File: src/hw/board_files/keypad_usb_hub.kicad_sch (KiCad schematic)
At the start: 2 parts, among them U1 MDBT50Q-1MV2, U2 IS31FL3731-SA

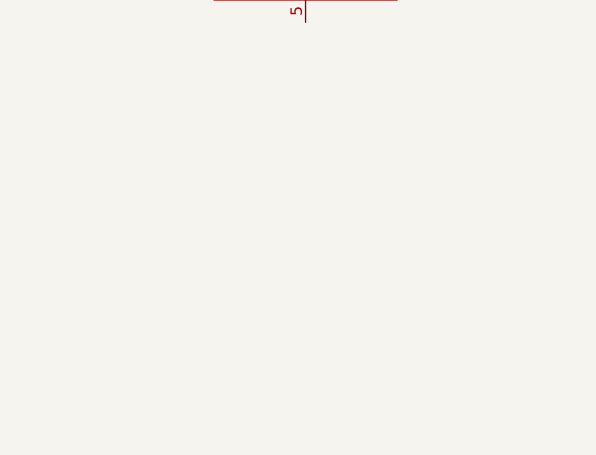
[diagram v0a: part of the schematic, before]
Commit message: Changed some ICs
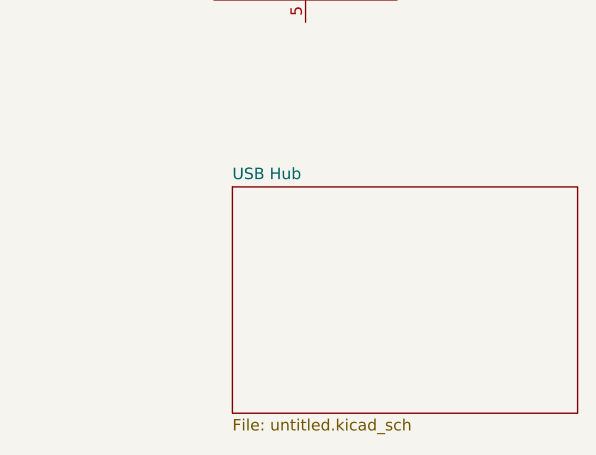
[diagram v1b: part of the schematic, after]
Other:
- added sheet USB Hub (untitled.kicad_sch)
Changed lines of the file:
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@@
+		)
+	)
+	(sheet
+		(at 188.722 109.728)
+		(size 38.354 25.146)
+		(exclude_from_sim no)
+		(in_bom yes)
+		(on_board yes)
+		(dnp no)
+		(fields_autoplaced yes)
+		(stroke
+			(width 0.1524)
+			(type solid)
+		)
+		(fill
+			(color 0 0 0 0.0000)
+		)
+		(property "Sheetname" "USB Hub"
+			(at 188.722 109.0164 0)
+			(effects
+				(font
+					(size 1.27 1.27)
+				)
+				(justify left bottom)
+			)
+		)
+		(property "Sheetfile" "untitled.kicad_sch"
+			(at 188.722 135.4586 0)
+			(effects
+				(font
+					(size 1.27 1.27)
+				)
+				(justify left top)
+			)
+		)
+		(instances
+			(project "keypad_usb_hub"
+				(path "/62136966-d911-451f-9518-a7827b282fe3"
+					(page "2")
+				)
+			)
 		)
 	)

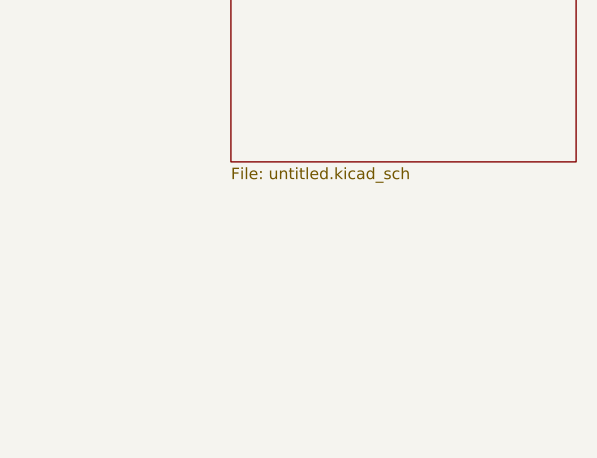
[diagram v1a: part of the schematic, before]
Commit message: Made USB hub symbol
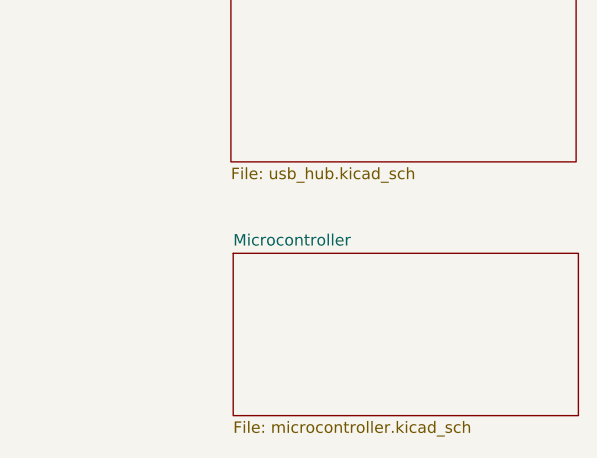
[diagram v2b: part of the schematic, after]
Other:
- added sheet Microcontroller (microcontroller.kicad_sch)
- sheet USB Hub: file untitled.kicad_sch -> usb_hub.kicad_sch
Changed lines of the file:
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@@
 			)
 		)
-		(property "Sheetfile" "untitled.kicad_sch"
+		(property "Sheetfile" "usb_hub.kicad_sch"
 			(at 188.722 135.4586 0)
 			(effects
@@
 				)
 			)
+		)
+	)
+	(sheet
+		(at 188.976 145.034)
+		(size 38.354 18.034)
+		(exclude_from_sim no)
+		(in_bom yes)
+		(on_board yes)
+		(dnp no)
+		(fields_autoplaced yes)
+		(stroke
+			(width 0.1524)
+			(type solid)
+		)
+		(fill
+			(color 0 0 0 0.0000)
+		)
+		(property "Sheetname" "Microcontroller"
+			(at 188.976 144.3224 0)
+			(effects
+				(font
+					(size 1.27 1.27)
+				)
+				(justify left bottom)
+			)
+		)
+		(property "Sheetfile" "microcontroller.kicad_sch"
+			(at 188.976 163.6526 0)
+			(effects
+				(font
+					(size 1.27 1.27)
+				)
+				(justify left top)
+			)
+		)
+		(instances
+			(project "keypad_usb_hub"
+				(path "/62136966-d911-451f-9518-a7827b282fe3"
+					(page "3")
+				)
+			)

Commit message: Schematic progress
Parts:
- removed U1: MDBT50Q-1MV2, RF_Module:Raytac_MDBT50Q, symbol RF_Module:MDBT50Q-1MV2
- removed U2: IS31FL3731-SA, Package_SO:SSOP-28_5.3x10.2mm_P0.65mm, symbol Driver_LED:IS31FL3731-SA
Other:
- sheet USB Hub renamed USB Hub Controller
- added sheet Power (power.kicad_sch)
- added sheet Receptacles (receptacles.kicad_sch)

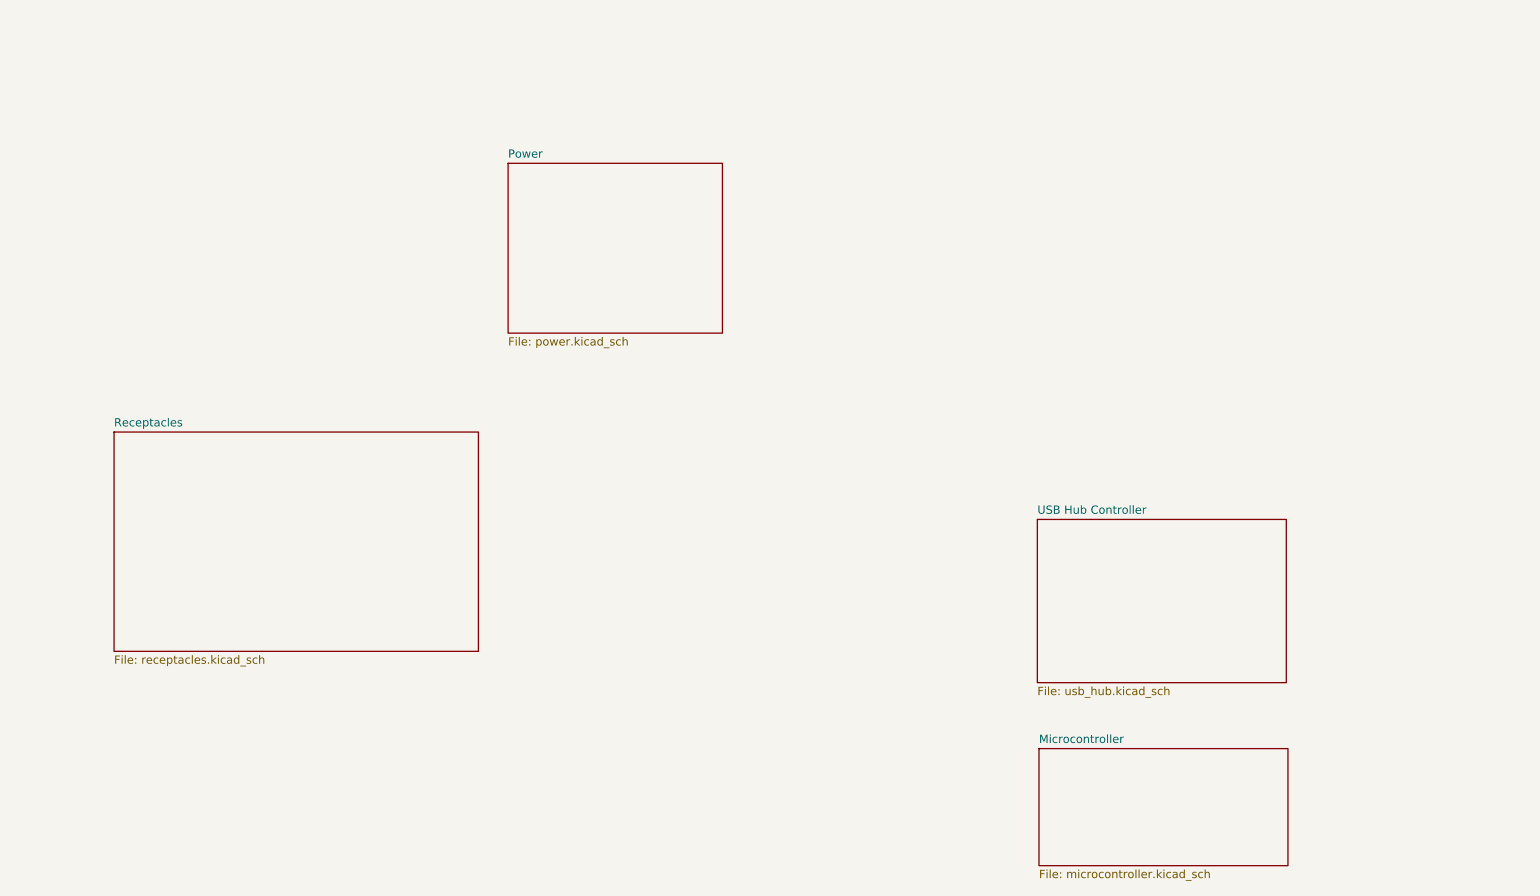
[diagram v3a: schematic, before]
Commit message: Finishing schematic. Need to review and clean up
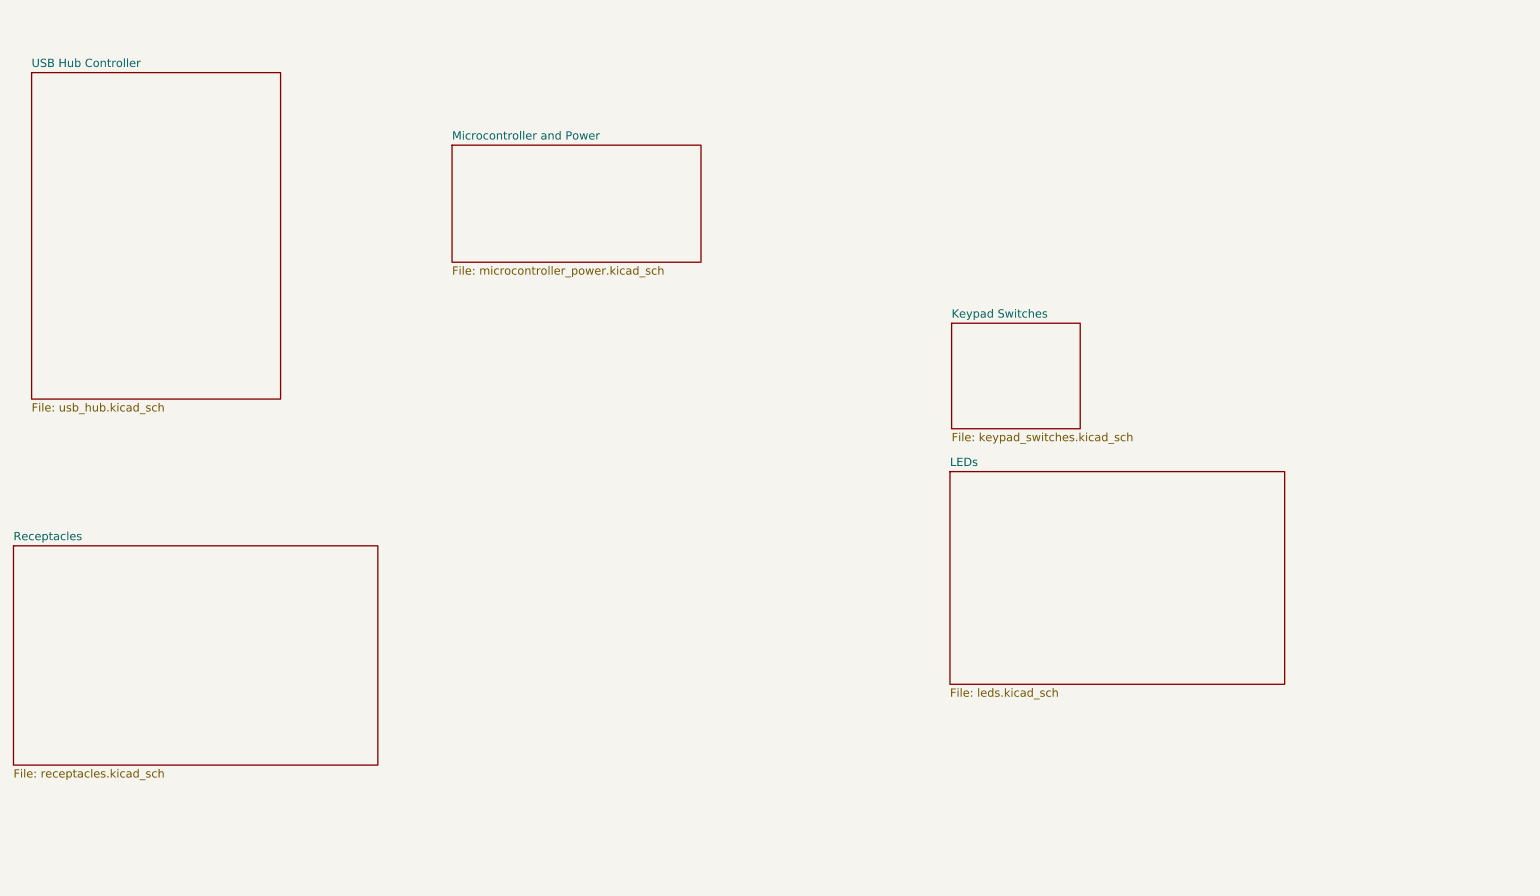
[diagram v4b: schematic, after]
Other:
- sheet Microcontroller renamed Microcontroller and Power
- removed sheet Power
- added sheet Keypad Switches (keypad_switches.kicad_sch)
- added sheet LEDs (leds.kicad_sch)
- sheet Microcontroller and Power: file microcontroller.kicad_sch -> microcontroller_power.kicad_sch
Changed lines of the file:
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@@
 	)
 	(sheet
-		(at 188.722 109.728)
-		(size 38.354 25.146)
+		(at 175.26 102.362)
+		(size 51.562 32.766)
+		(exclude_from_sim no)
+		(in_bom yes)
+		(on_board yes)
+		(dnp no)
+		(fields_autoplaced yes)
+		(stroke
+			(width 0.1524)
+			(type solid)
+		)
+		(fill
+			(color 0 0 0 0.0000)
+		)
+		(property "Sheetname" "LEDs"
+			(at 175.26 101.6504 0)
+			(effects
+				(font
+					(size 1.27 1.27)
+				)
+				(justify left bottom)
+			)
+		)
+		(property "Sheetfile" "leds.kicad_sch"
+			(at 175.26 135.7126 0)
+			(effects
+				(font
+					(size 1.27 1.27)
+				)
+				(justify left top)
+			)
+		)
+		(instances
+			(project "keypad_usb_hub"
+				(path "/62136966-d911-451f-9518-a7827b282fe3"
+					(page "5")
+				)
+			)
+		)
+	)
+	(sheet
+		(at 33.782 40.894)
+		(size 38.354 50.292)
 		(exclude_from_sim no)
 		(in_bom yes)
@@
 		)
 		(property "Sheetname" "USB Hub Controller"
-			(at 188.722 109.0164 0)
+			(at 33.782 40.1824 0)
 			(effects
 				(font
@@
 		)
 		(property "Sheetfile" "usb_hub.kicad_sch"
-			(at 188.722 135.4586 0)
+			(at 33.782 91.7706 0)
 			(effects
 				(font
@@
 	)
 	(sheet
-		(at 188.976 145.034)
+		(at 98.552 52.07)
 		(size 38.354 18.034)
 		(exclude_from_sim no)
@@
 			(color 0 0 0 0.0000)
 		)
-		(property "Sheetname" "Microcontroller"
-			(at 188.976 144.3224 0)
-			(effects
-				(font
-					(size 1.27 1.27)
-				)
-				(justify left bottom)
-			)
-		)
-		(property "Sheetfile" "microcontroller.kicad_sch"
-			(at 188.976 163.6526 0)
+		(property "Sheetname" "Microcontroller and Power"
+			(at 98.552 51.3584 0)
+			(effects
+				(font
+					(size 1.27 1.27)
+				)
+				(justify left bottom)
+			)
+		)
+		(property "Sheetfile" "microcontroller_power.kicad_sch"
+			(at 98.552 70.6886 0)
 			(effects
 				(font
@@
 	)
 	(sheet
-		(at 46.482 96.266)
+		(at 30.988 113.792)
 		(size 56.134 33.782)
 		(exclude_from_sim no)
@@
 		)
 		(property "Sheetname" "Receptacles"
-			(at 46.482 95.5544 0)
+			(at 30.988 113.0804 0)
 			(effects
 				(font
@@
 		)
 		(property "Sheetfile" "receptacles.kicad_sch"
-			(at 46.482 130.6326 0)
+			(at 30.988 148.1586 0)
 			(effects
 				(font
@@
 	)
 	(sheet
-		(at 107.188 54.864)
-		(size 33.02 26.162)
-		(exclude_from_sim no)
-		(in_bom yes)
-		(on_board yes)
-		(dnp no)
-		(fields_autoplaced yes)
-		(stroke
-			(width 0.1524)
-			(type solid)
-		)
-		(fill
-			(color 0 0 0 0.0000)
-		)
-		(property "Sheetname" "Power"
-			(at 107.188 54.1524 0)
-			(effects
-				(font
-					(size 1.27 1.27)
-				)
-				(justify left bottom)
-			)
-		)
-		(property "Sheetfile" "power.kicad_sch"
-			(at 107.188 81.6106 0)
-			(effects
-				(font
-					(size 1.27 1.27)
-				)
-				(justify left top)
-			)
-		)
-		(instances
-			(project "keypad_usb_hub"
-				(path "/62136966-d911-451f-9518-a7827b282fe3"
-					(page "5")
-				)
-			)
+		(at 175.514 79.502)
+		(size 19.812 16.256)
+		(exclude_from_sim no)
+		(in_bom yes)
+		(on_board yes)
+		(dnp no)
+		(fields_autoplaced yes)
+		(stroke
+			(width 0.1524)
+			(type solid)
+		)
+		(fill
+			(color 0 0 0 0.0000)
+		)
+		(property "Sheetname" "Keypad Switches"
+			(at 175.514 78.7904 0)
+			(effects
+				(font
+					(size 1.27 1.27)
+				)
+				(justify left bottom)
+			)
+		)
+		(property "Sheetfile" "keypad_switches.kicad_sch"
+			(at 175.514 96.3426 0)
+			(effects
+				(font
+					(size 1.27 1.27)
+				)
+				(justify left top)
+			)
+		)
+		(instances
+			(project "keypad_usb_hub"
+				(path "/62136966-d911-451f-9518-a7827b282fe3"
+					(page "6")
+				)
+			)

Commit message: Added all footprints, need to connect switches to MCU
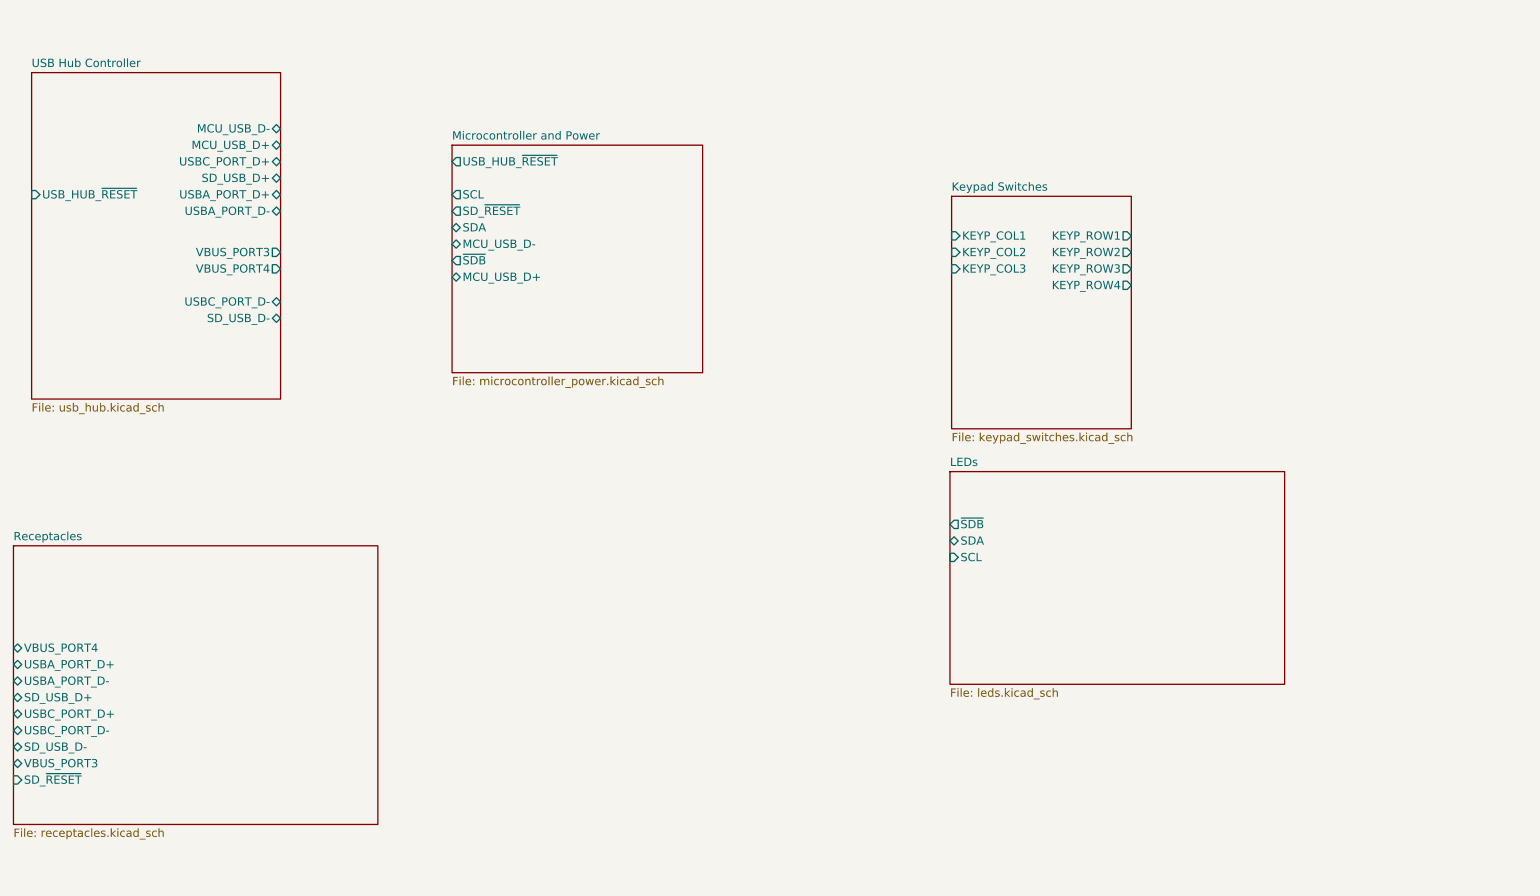
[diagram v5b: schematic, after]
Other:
- sheet Keypad Switches ports: added KEYP_COL1, KEYP_COL2, KEYP_COL3, KEYP_ROW1, KEYP_ROW2, KEYP_ROW3, KEYP_ROW4; removed none
- sheet LEDs ports: added SCL, SDA, ~{SDB}; removed none
- sheet Microcontroller and Power ports: added MCU_USB_D+, MCU_USB_D-, SCL, SDA, SD_~{RESET}, USB_HUB_~{RESET}, ~{SDB}; removed none
- sheet Receptacles ports: added SD_USB_D+, SD_USB_D-, SD_~{RESET}, USBA_PORT_D+, USBA_PORT_D-, USBC_PORT_D+, USBC_PORT_D-, VBUS_PORT3, VBUS_PORT4; removed none
- sheet USB Hub Controller ports: added MCU_USB_D+, MCU_USB_D-, SD_USB_D+, SD_USB_D-, USBA_PORT_D+, USBA_PORT_D-, USBC_PORT_D+, USBC_PORT_D-, USB_HUB_~{RESET}, VBUS_PORT3, VBUS_PORT4; removed none

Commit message: Added rotary encoder and OLED. Started laying out board then I need to review schematic and change pinout if needed
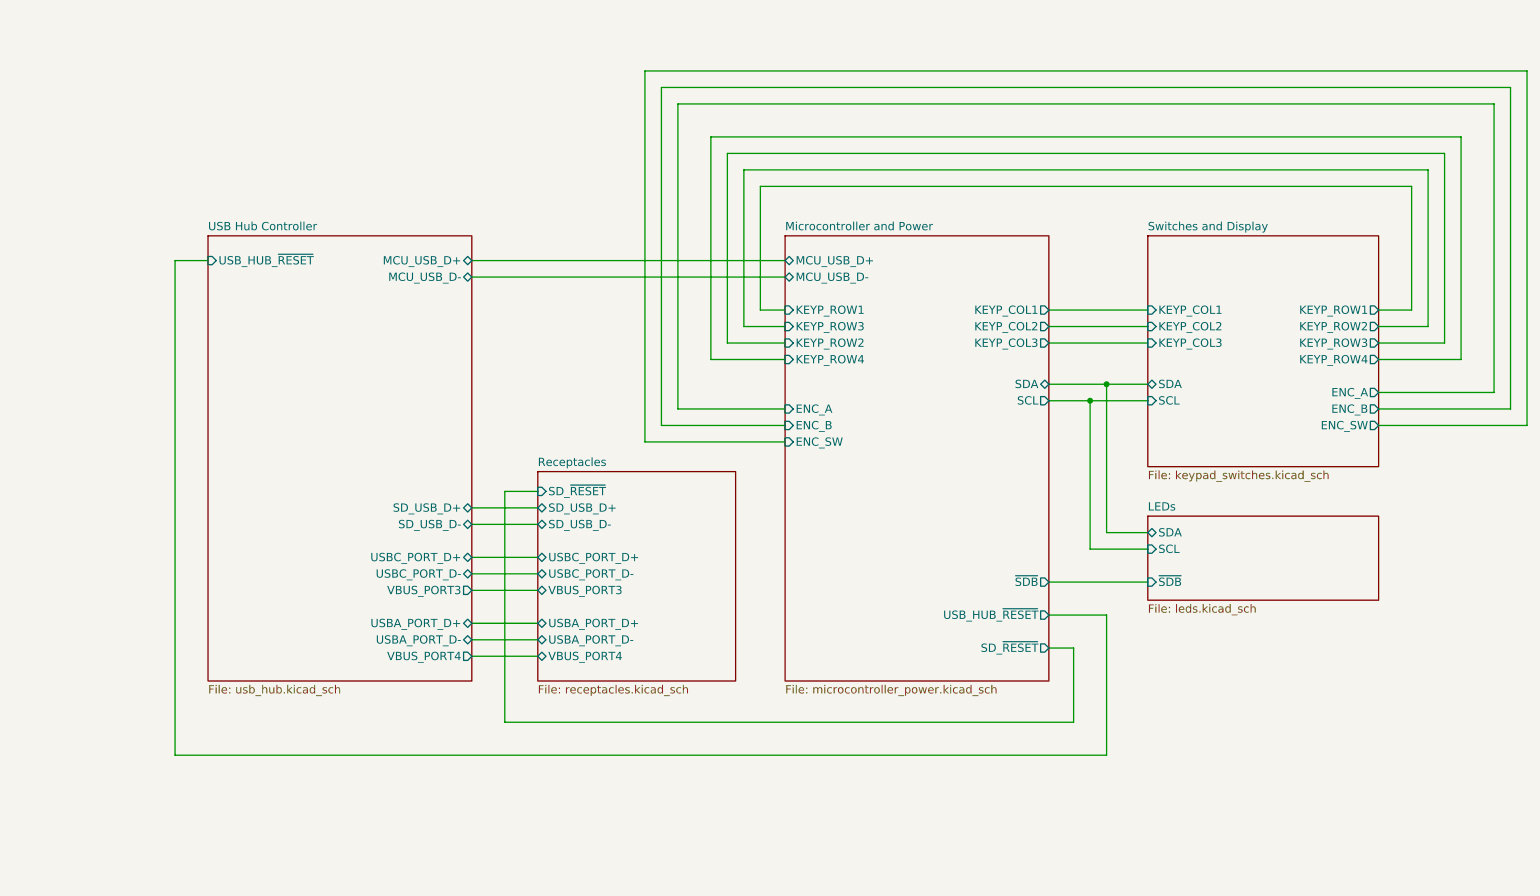
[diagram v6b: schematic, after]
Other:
- sheet Keypad Switches renamed Switches and Display
- sheet Microcontroller and Power ports: added ENC_A, ENC_B, ENC_SW, KEYP_COL1, KEYP_COL2, KEYP_COL3, KEYP_ROW1, KEYP_ROW2, KEYP_ROW3, KEYP_ROW4; removed none
- sheet Switches and Display ports: added ENC_A, ENC_B, ENC_SW, SCL, SDA; removed none
